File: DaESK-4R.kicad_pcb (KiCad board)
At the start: 2 copper layers, 124.1 x 97 mm, 115 parts, among them J1 AudioJack4, J3 Conn_01x06, J5 Conn_01x11, J7 Conn_01x06, SW2 SW_Push, U2 ATmega32U4, U4 IS31FL3737, X1 XRCGB16M000FXN00R0

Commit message: Update DaESK-4R.kicad_pcb
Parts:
- moved C1 1.52 mm to (203.1, 29.9)
- moved R1 1.52 mm to (203.1, 28.3)
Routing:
- net Net-(C1-Pad1): track 3.80 -> 6.28 mm

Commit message: 4R updated placement of MCU
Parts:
- added LED_2: STATUS_LED, LED_SMD:LED_0603_1608Metric, F.Cu at (169.3, 28.7)
- added R7: 33, Resistor_SMD:R_0603_1608Metric, B.Cu at (169.3, 28.7)
- added SW1: Reset, SamacSys_Parts:EVPBB2A9B000, B.Cu at (160.2, 29.0)
- C1: value 0u1F -> 0u1
- C10: footprint Capacitor_SMD:C_0805_2012Metric_Pad1.15x1.40mm_HandSolder -> Capacitor_SMD:C_0805_2012Metric; moved to B.Cu
- C11: footprint Capacitor_SMD:C_0805_2012Metric_Pad1.15x1.40mm_HandSolder -> Capacitor_SMD:C_0805_2012Metric
- C12, JP6: moved to F.Cu
- C17, C3: footprint Capacitor_Tantalum_SMD:CP_EIA-3216-18_Kemet-A_Pad1.58x1.35mm_HandSolder -> Capacitor_Tantalum_SMD:CP_EIA-3216-18_Kemet-A
- C2R1, C2R2, C2R3, C2R4, C3R1, C3R2, C3R3, C3R4, C4R1, C4R2, C4R3, C4R4, C5R1, C5R2, C5R3, C5R4, C6R1, C6R2, C6R3, C6R4, C7R1, C7R2, C7R3, C7R4: footprint Keyboard 2:Kailh_socket_MX_reversible_v2 -> Keyboard Library:Kailh_socket_MX_reversible_v2
- C7, C8, JP5, R13: moved to B.Cu
- F1: footprint Fuse:Fuse_0805_2012Metric_Pad1.15x1.40mm_HandSolder -> Fuse:Fuse_0603_1608Metric
- J1: value AudioJack4 -> TRRS; footprint Keyboard 2:TRRS-PJ-320A-reversible -> Keyboard Library:TRRS-PJ-320A-reversible
- LED_1: renamed from POWER_LED1; value LED_Small -> PWR_LED; footprint LED_SMD:LED_0603_1608Metric_Pad1.05x0.95mm_HandSolder -> LED_SMD:LED_0603_1608Metric
- R6: value 10K -> 10k
- R9: value 4K7 -> 4k7
- RGB_C2R1: value 5-ABC -> RGB; footprint Keyboard 2:LEDSC160X160X070-4N_reversible -> Keyboard Library:LEDSC160X160X070-4N_reversible
- RGB_C2R2: value 6-ABC -> RGB; footprint Keyboard 2:LEDSC160X160X070-4N_reversible -> Keyboard Library:LEDSC160X160X070-4N_reversible
- RGB_C2R3: value 7-ABC -> RGB; footprint Keyboard 2:LEDSC160X160X070-4N_reversible -> Keyboard Library:LEDSC160X160X070-4N_reversible
- RGB_C2R4: value 8-ABC -> RGB; footprint Keyboard 2:LEDSC160X160X070-4N_reversible -> Keyboard Library:LEDSC160X160X070-4N_reversible
- RGB_C3R1: value 9-ABC -> RGB; footprint Keyboard 2:LEDSC160X160X070-4N_reversible -> Keyboard Library:LEDSC160X160X070-4N_reversible
- RGB_C3R2: value 10-ABC -> RGB; footprint Keyboard 2:LEDSC160X160X070-4N_reversible -> Keyboard Library:LEDSC160X160X070-4N_reversible
- RGB_C3R3: value 11-ABC -> RGB; footprint Keyboard 2:LEDSC160X160X070-4N_reversible -> Keyboard Library:LEDSC160X160X070-4N_reversible
- RGB_C3R4: value 12-ABC -> RGB; footprint Keyboard 2:LEDSC160X160X070-4N_reversible -> Keyboard Library:LEDSC160X160X070-4N_reversible
- RGB_C4R1: value 1-DEF -> RGB; footprint Keyboard 2:LEDSC160X160X070-4N_reversible -> Keyboard Library:LEDSC160X160X070-4N_reversible
- RGB_C4R2: value 2-DEF -> RGB; footprint Keyboard 2:LEDSC160X160X070-4N_reversible -> Keyboard Library:LEDSC160X160X070-4N_reversible
- RGB_C4R3: value 3-DEF -> RGB; footprint Keyboard 2:LEDSC160X160X070-4N_reversible -> Keyboard Library:LEDSC160X160X070-4N_reversible
- RGB_C4R4: value 4-DEF -> RGB; footprint Keyboard 2:LEDSC160X160X070-4N_reversible -> Keyboard Library:LEDSC160X160X070-4N_reversible
- RGB_C5R1: value 5-DEF -> RGB; footprint Keyboard 2:LEDSC160X160X070-4N_reversible -> Keyboard Library:LEDSC160X160X070-4N_reversible
- RGB_C5R2: value 6-DEF -> RGB; footprint Keyboard 2:LEDSC160X160X070-4N_reversible -> Keyboard Library:LEDSC160X160X070-4N_reversible
- RGB_C5R3: value 7-DEF -> RGB; footprint Keyboard 2:LEDSC160X160X070-4N_reversible -> Keyboard Library:LEDSC160X160X070-4N_reversible
- RGB_C5R4: value 8-DEF -> RGB; footprint Keyboard 2:LEDSC160X160X070-4N_reversible -> Keyboard Library:LEDSC160X160X070-4N_reversible
- RGB_C6R1: value CB1_9 -> RGB; footprint Keyboard 2:LEDSC160X160X070-4N_reversible -> Keyboard Library:LEDSC160X160X070-4N_reversible
- RGB_C6R2: value CB1_8 -> RGB; footprint Keyboard 2:LEDSC160X160X070-4N_reversible -> Keyboard Library:LEDSC160X160X070-4N_reversible
- RGB_C6R3: value CB1_7 -> RGB; footprint Keyboard 2:LEDSC160X160X070-4N_reversible -> Keyboard Library:LEDSC160X160X070-4N_reversible
- RGB_C6R4: value CB1_6 -> RGB; footprint Keyboard 2:LEDSC160X160X070-4N_reversible -> Keyboard Library:LEDSC160X160X070-4N_reversible
- RGB_C7R1: value CB2_1 -> RGB; footprint Keyboard 2:LEDSC160X160X070-4N_reversible -> Keyboard Library:LEDSC160X160X070-4N_reversible
- RGB_C7R2: value CB2_2 -> RGB; footprint Keyboard 2:LEDSC160X160X070-4N_reversible -> Keyboard Library:LEDSC160X160X070-4N_reversible
- RGB_C7R3: value CB2_3 -> RGB; footprint Keyboard 2:LEDSC160X160X070-4N_reversible -> Keyboard Library:LEDSC160X160X070-4N_reversible
- RGB_C7R4: value CB2_4 -> RGB; footprint Keyboard 2:LEDSC160X160X070-4N_reversible -> Keyboard Library:LEDSC160X160X070-4N_reversible
- SW2: value SW_Push -> Reset; footprint Keyboard Library:2-pin_reset_switch -> SamacSys_Parts:EVPBB2A9B000
- moved SW2 27.0 mm to (160.2, 29.0)
- moved J3 17.0 mm to (165.9, 27.9)
- moved R6 16.1 mm to (163.8, 28.7)
- moved C7 15.9 mm to (165.9, 40.9), turned to 0 degrees
- moved C6 15.1 mm to (164.1, 33.6)
- moved X1 14.7 mm to (161.9, 33.1), turned to 270 degrees
- moved C10 14.6 mm to (169.6, 32.3), turned to 180 degrees
- moved J1 14.4 mm to (152.4, 38.3), turned to 90 degrees
- moved R10 13.6 mm to (153.4, 33.5), turned to 90 degrees
- moved JP3 13.6 mm to (157.4, 43.7), turned to 180 degrees
- moved JP4 13.6 mm to (157.4, 43.7), turned to 180 degrees
- moved ZD1 13.5 mm to (174.2, 28.7), turned to 0 degrees
- moved R9 12.8 mm to (154.9, 33.5), turned to 270 degrees
- moved F1 12.4 mm to (177.3, 31.0), turned to 270 degrees
- moved C5 12.3 mm to (164.1, 36.6), turned to 270 degrees
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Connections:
- J1 pad R1: I2C- -> I2C+
- J1 pad R2: I2C+ -> I2C-
- SW2 pad 1: GND -> RESET
- SW2 pad 2: RESET -> GND
- U2 pad 25: COL_TH1 -> ROW_4
- U2 pad 26: COL_TH2 -> COL_TH1
- U2 pad 27: ROW_4 -> COL_TH2
- U2 pad 8: (no net) -> /MCU/LED
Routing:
- net I2C+: track 169.3 -> 148.0 mm
- net VCC: track 205.7 -> 222.8 mm, vias 12 -> 10
- net GND: track 71.6 -> 63.3 mm, vias 146 -> 138
- net ROW_2: track 194.3 -> 187.5 mm
- net COL_B: track 44.1 -> 38.2 mm
- net ROW_3: track 200.4 -> 194.5 mm
- net COL_A: track 31.2 -> 25.8 mm
- net COL_TH1: track 68.4 -> 63.3 mm
- net COL_TH2: track 68.9 -> 64.1 mm
- net ROW_1: track 186.0 -> 181.3 mm, vias 12 -> 13
- net /MCU/LED: track 0.00 -> 4.64 mm
- net VCC_USB: track 14.3 -> 18.8 mm, vias 3 -> 2
- net I2C-: track 160.1 -> 156.0 mm
- net S: track 5.93 -> 9.94 mm, vias 0 -> 1
- net /MCU/HAND: track 7.21 -> 10.7 mm
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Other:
- outline, holes or cut-outs redrawn

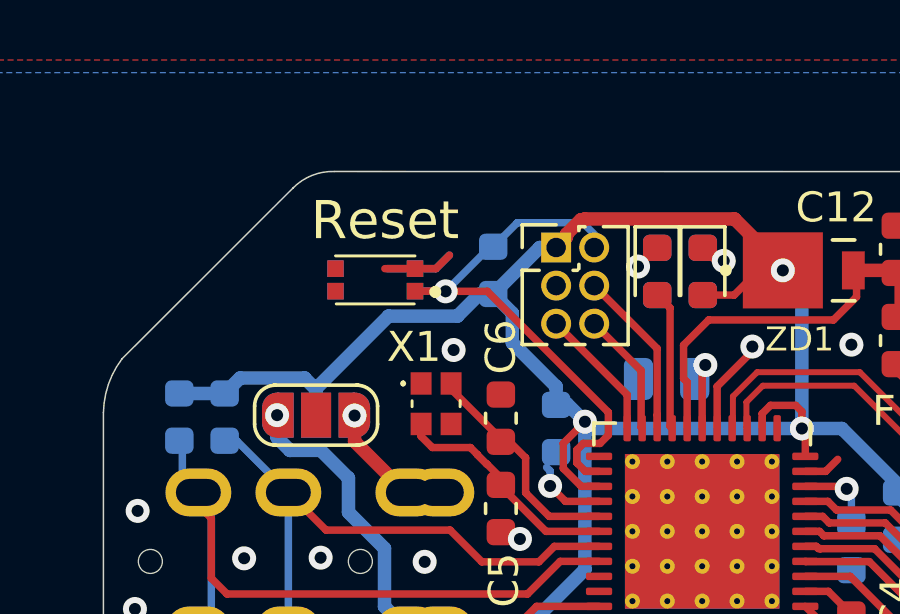
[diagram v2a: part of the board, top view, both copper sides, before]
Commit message: fixed reset switch
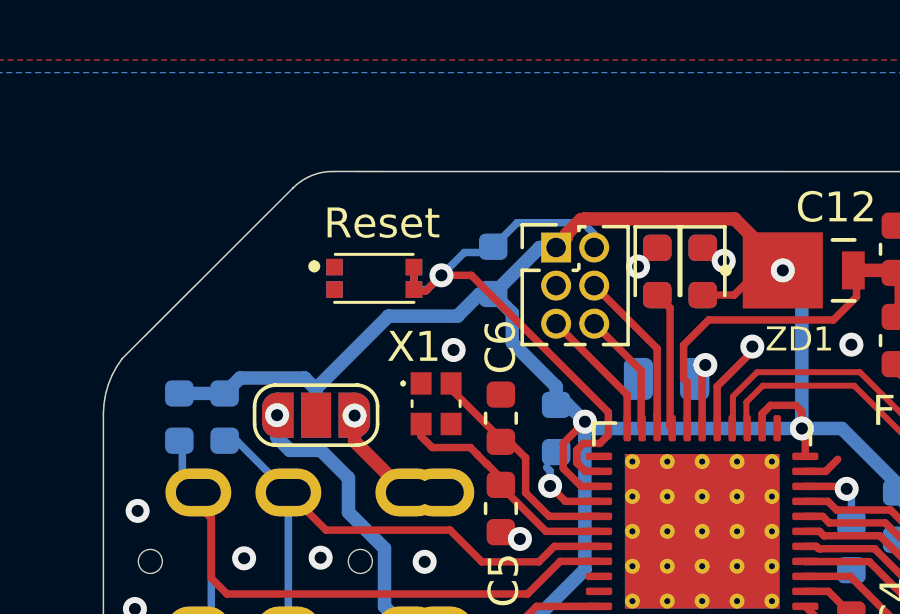
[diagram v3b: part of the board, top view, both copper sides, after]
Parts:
- removed SW1, SW2: Reset, SamacSys_Parts:EVPBB2A9B000
- added S1: Reset, SamacSys_Parts:EVPBB2A9B000, F.Cu at (159.6, 28.9)
- added S2: Reset, SamacSys_Parts:EVPBB2A9B000, B.Cu at (159.6, 28.9)
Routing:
- net GND: track 63.3 -> 58.6 mm
- net RESET: track 18.8 -> 20.7 mm
